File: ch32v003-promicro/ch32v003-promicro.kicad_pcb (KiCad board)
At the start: 2 copper layers, 17.8 x 33 mm, 21 parts, among them J1 USB2.0_C_v3, J2 SWD-MCU_Side-10Pin, J3 ProMicro-LeftPin, J4 ProMicro-RightPin, J5 SWD, SW1 SW_Push, U1 AMS1117-3.3, U2 CH32V003F4P6, U3 CH213K

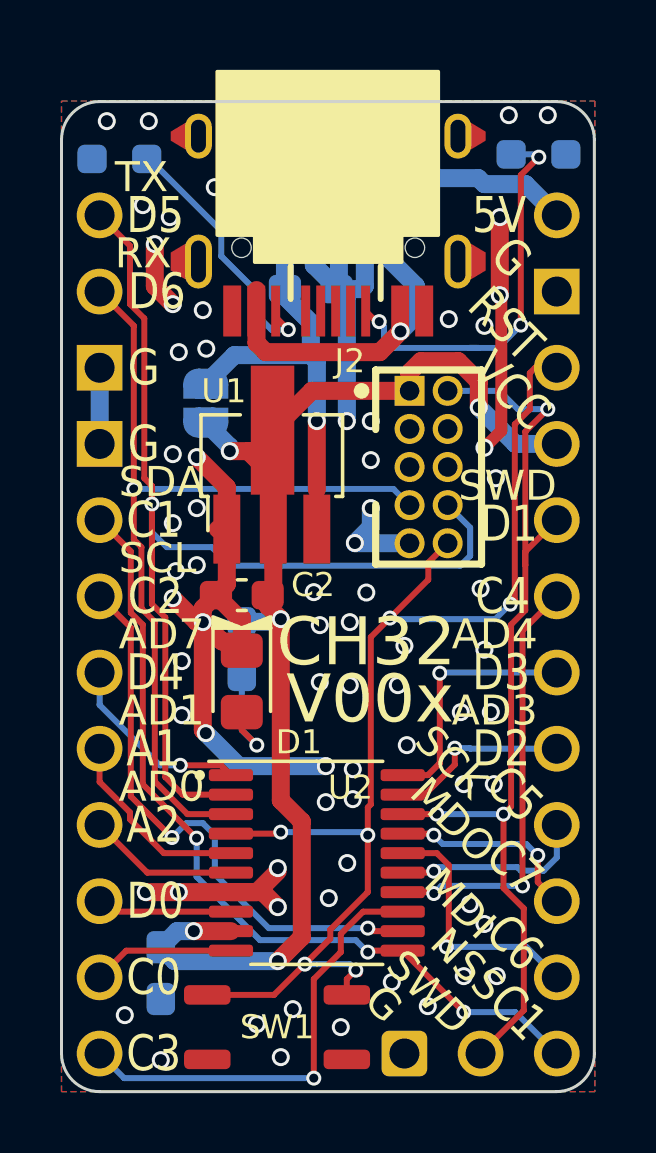
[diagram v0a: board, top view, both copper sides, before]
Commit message: revert to ch32v003 v1.2.0
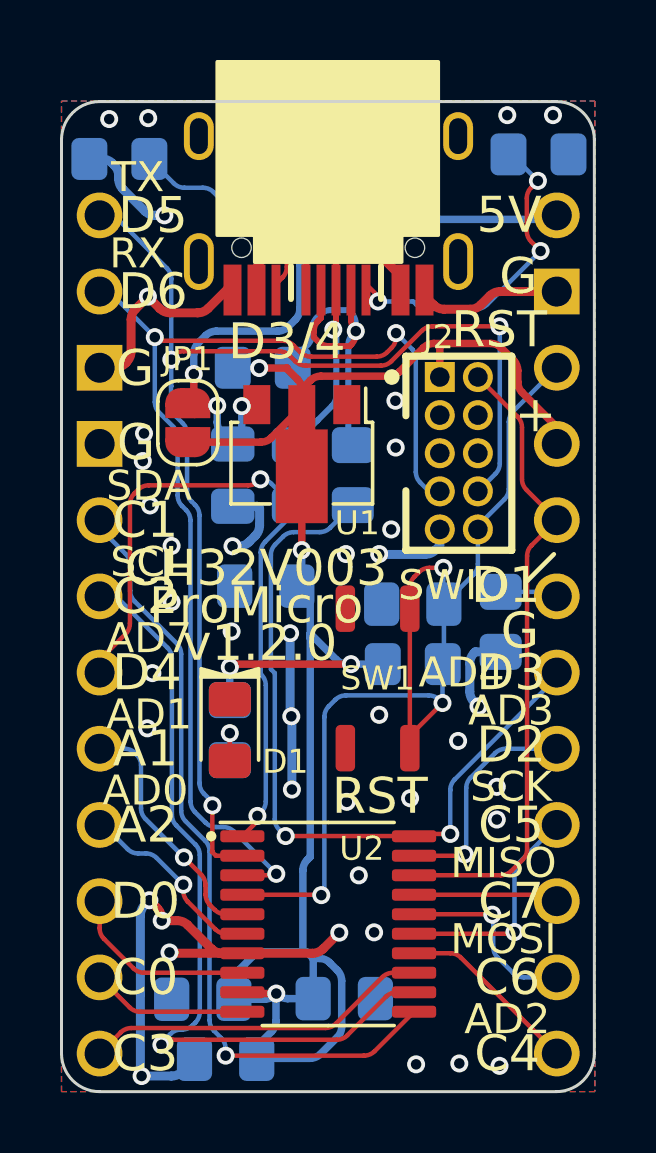
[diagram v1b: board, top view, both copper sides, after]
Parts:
- removed J5: SWD, 74th:PinOut_Pin_2_2GND
- added C3: 100n, 74th:Capacitor_0805_2012, B.Cu at (109.5, 79.0)
- added C5: 100n, 74th:Capacitor_0805_2012, B.Cu at (102.5, 92.2)
- added C6: 1u, 74th:Capacitor_0805_2012, B.Cu at (103.3, 94.2)
- added R5: 1.5k(NC), 74th:Register_0805_2012, B.Cu at (104.5, 71.1)
- added R6: 27.4(NC), 74th:Register_0805_2012, B.Cu at (107.5, 74.7)
- added R7: 27.4(NC), 74th:Register_0805_2012, B.Cu at (105.5, 74.7)
- added R8: 0, 74th:Register_0805_2012, B.Cu at (112.4, 79.6)
- added R9: 10k, 74th:Register_0805_2012, B.Cu at (109.5, 81.0)
- C1, C4: footprint 74th:Capacitor_0603_1608 -> 74th:Capacitor_0805_2012
- C2: footprint 74th:Capacitor_0603_1608 -> 74th:Capacitor_0805_2012; moved to B.Cu
- JP1: footprint 74th:SolderJumper-2 -> Jumper:SolderJumper-2_P1.3mm_Open_RoundedPad1.0x1.5mm; moved to F.Cu
- R10, R3, R4: footprint 74th:Register_0603_1608 -> 74th:Register_0805_2012
- SW1: footprint 74th:Switch_SKRPABE010 -> 74th:PushButton_SKRPABE010
- moved SW1 12.1 mm to (108.3, 81.5), turned to 90 degrees
- moved G*** 7.93 mm to (110.4, 86.0)
- moved C1 6.69 mm to (103.5, 74.7), turned to -90 degrees
- moved C4 6.19 mm to (107.2, 92.2), turned to 0 degrees
- moved R10 2.73 mm to (103.4, 83.2)
- moved U2 2.07 mm to (106.7, 89.7)
- moved D1 1.67 mm to (103.4, 83.2)
- moved U3 1.62 mm to (107.2, 66.0), turned to 180 degrees
- moved J2 1.11 mm to (110.4, 71.4)
- moved U1 1.03 mm to (105.8, 74.3), turned to -90 degrees
- moved JP1 0.88 mm to (102.0, 73.0)
- moved C2 0.76 mm to (104.6, 78.4)
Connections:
- net /PA1 renamed /5
- net /PA2 renamed /6/A7
- net /PC0 renamed /8/A8
- net /PC2 renamed /3/I2C_SCL
- net /PC3 renamed /9/A9
- net /PC5 renamed /15/SPI_SCK
- net /PC6 renamed /16/SPL_MOSI
- net /PC7 renamed /14/SPI_MISO
- net /PD0 renamed /7
- net /PD1 renamed /21/A3
- net /PD2 renamed /18/A0
- net /PD3 renamed /19/A1
- net /PD4 renamed /4/A6
- net /PD5 renamed /1/UART_TX
- net /PD6 renamed /0/UART_RX
- J1 pad 2: unconnected-(J1-D--Pad2) -> /USB_D-
- J1 pad 3: unconnected-(J1-D+-Pad3)_1 -> /USB_D+
- J3 pad 5: /PC1 -> /2/I2C_SDA
- J4 pad 1: /PC1 -> /10/A10
- J4 pad 7: /PC4 -> /20/A2
- U2 pad 11: /PC1 -> /2/I2C_SDA
- U2 pad 14: /PC4 -> /10/A10
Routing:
- net /PC1: track 27.7 -> 0.00 mm, vias 3 -> 0
- net /2/I2C_SDA: track 0.00 -> 26.0 mm, vias 0 -> 1
- net VCC: track 42.4 -> 61.6 mm
- net /4/A6: track 6.43 -> 23.2 mm, vias 1 -> 2
- net /19/A1: track 8.31 -> 25.1 mm, vias 1 -> 2
- net /PC4: track 15.0 -> 0.00 mm, vias 2 -> 0
- net GND: track 59.0 -> 44.8 mm, vias 82 -> 46
- net /USB_D-: track 0.00 -> 12.2 mm, vias 0 -> 1
- net /21/A3: track 32.3 -> 21.4 mm, vias 3 -> 0
- net /USB_D+: track 0.00 -> 9.03 mm, vias 0 -> 1
- net /0/UART_RX: track 29.5 -> 37.5 mm, vias 1 -> 3
- net +5V: track 27.0 -> 19.3 mm, vias 1 -> 3
- net /10/A10: track 0.00 -> 6.12 mm
- net /3/I2C_SCL: track 19.2 -> 25.2 mm, vias 2 -> 1
- net Net-(J1-VBUS): track 13.4 -> 8.08 mm
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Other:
- board text added: "+"
- board text added: "AD2"
- board text added: "CH32V003"
- board text added: "D3/4"
- board text added: "MISO"
- board text added: "MOSI"
- board text added: "SWIO"
- board text added: "USB"
- board text added: "v1.2.0"
- board text removed: "CH32"
- board text removed: "CH32V00x"
- board text removed: "MDI"
- board text removed: "MDO"
- board text removed: "NSS"
- board text removed: "SWD"
- board text removed: "V00x"
- board text removed: "VCC"
- board text removed: "VCC=5V"
- board text removed: "v${REVISION}"
